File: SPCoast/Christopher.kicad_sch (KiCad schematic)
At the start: 42 parts, among them SW9813 813, SW9815 815, SW9817 817, SW9900 815A

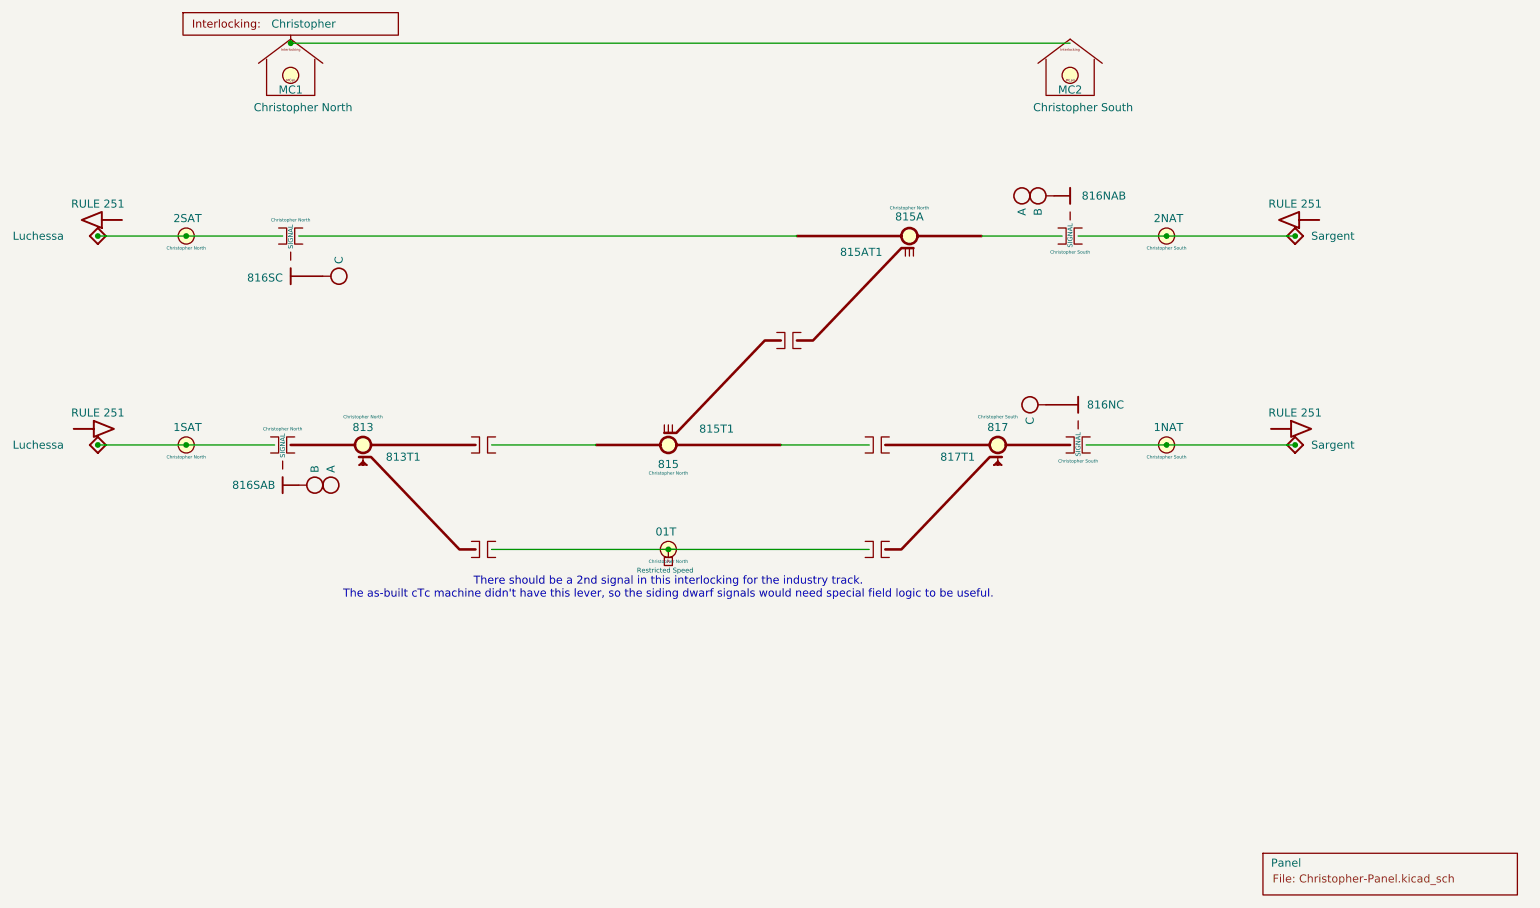
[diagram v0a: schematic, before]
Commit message: chore(kicad): SPCoast symbols refreshed, field attribute visibility, no-connects on unused pins (owner's edit, baseline)
Owner, 2026-10-08: updated symbols from the libraries (the field pin direction flip, InterlockingPlant
61269e0), adjusted attribute visibility, added 22 no-connect markers on unused pins.

Verified (committed as saved, no edits):
- 485 components, 648 nets; every net identical to the previous commit.
- ERC 53 -> 20 messages (13 errors, 7 warnings). Remaining: unconnected HOUSE H / aux MC pins
  (Gilroy Caltrain, Luchessa, Watsonville); Corporal SW11901 still Railroad:Switch_HandThrow (not in
  the library) with open N/R legs; Sargent switch 1 open N/R legs; Christopher Panel U10029 A6 open
  while lamp LMP10093 carries a no-connect; 5 inherited wire stubs.
- Every instance path starts at the root uuid.

Co-Authored-By: Claude Opus 5.5 <noreply@anthropic.com>
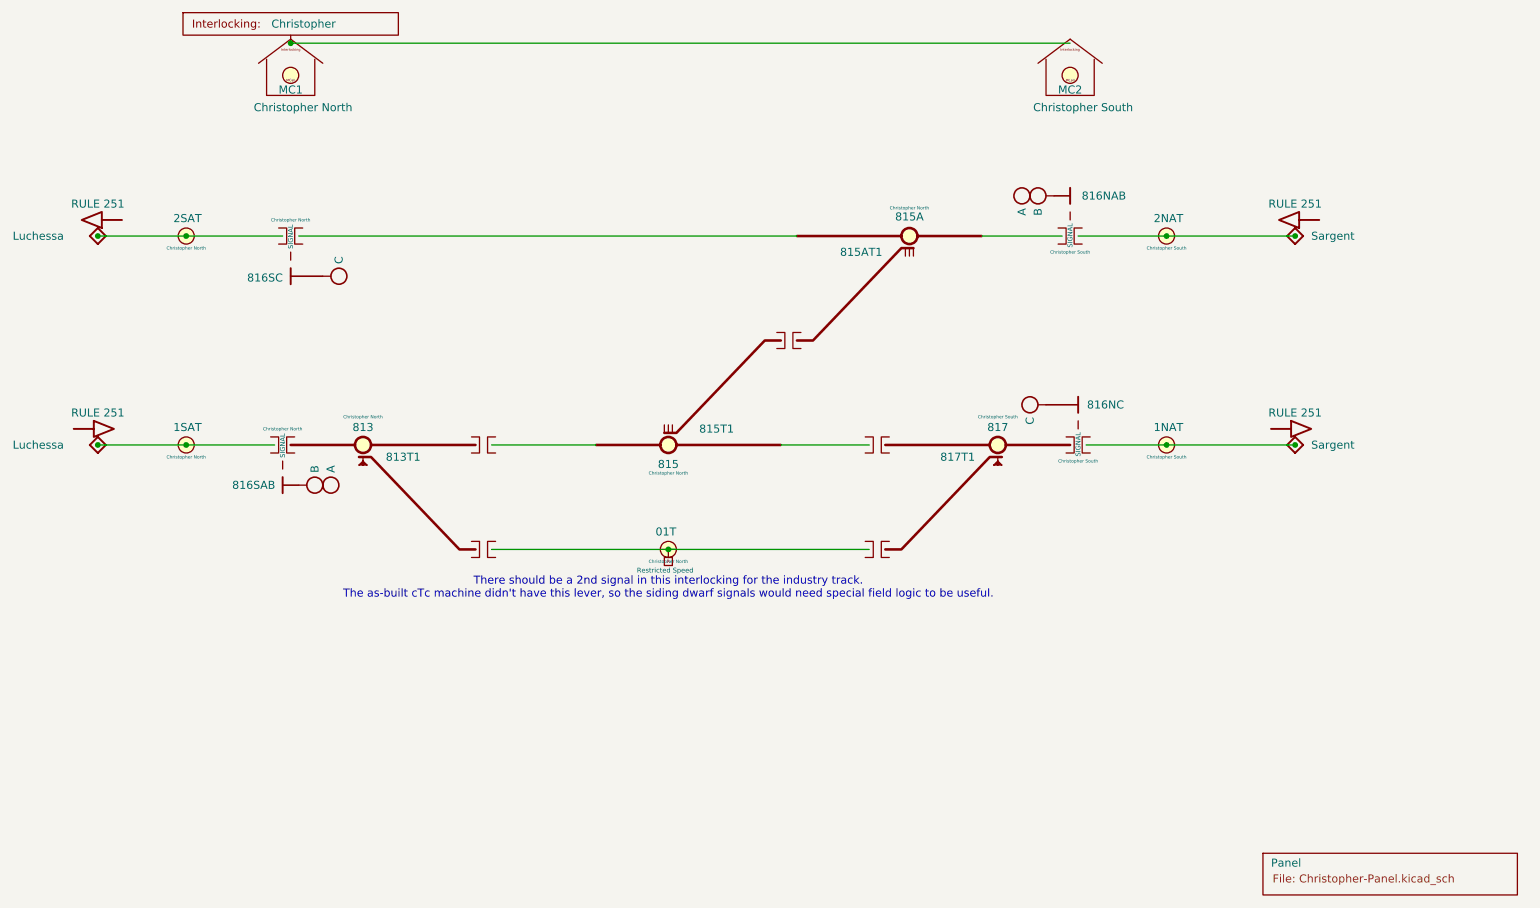
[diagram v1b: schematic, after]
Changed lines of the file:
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@@
 		)
 		(property "Milepost" "81.6"
-			(at 195.58 47.63 0)
+			(at 195.58 47.625 0)
 			(hide yes)
 			(show_name no)
@@
 		)
 		(property "CP" "Christopher North"
-			(at 55.88 102.23 0)
+			(at 55.88 102.235 0)
 			(show_name no)
 			(do_not_autoplace no)
@@
 		)
 		(property "CP" "Christopher North"
-			(at 132.08 104.78 0)
+			(at 132.08 104.775 0)
 			(show_name no)
 			(do_not_autoplace no)
@@
 			(at 139.7 97.79 0)
 			(show_name no)
-			(do_not_autoplace no)
+			(do_not_autoplace yes)
 			(effects
 				(font
@@
 		)
 		(property "Role" "APPLIANCE"
-			(at 132.08 100.33 0)
+			(at 123.825 92.71 0)
 			(hide yes)
 			(show_name no)
@@
 		)
 		(property "Kind" "SWITCH_REMOTE"
-			(at 132.08 100.33 0)
+			(at 126.365 94.615 0)
 			(hide yes)
 			(show_name no)
@@
 			)
 		)
+		(property "Indications" ""
+			(at 145.415 99.695 0)
+			(show_name no)
+			(do_not_autoplace no)
+			(effects
+				(font
+					(size 0.508 0.508)
+				)
+			)
+		)
 		(pin "2"
 		)
@@
 		)
 		(property "CP" "Christopher North"
-			(at 83.82 95.88 0)
+			(at 83.82 95.885 0)
 			(show_name no)
 			(do_not_autoplace no)
@@
 		)
 		(property "TC" "${VALUE}T1"
-			(at 90.17 102.23 0)
+			(at 90.17 102.235 0)
 			(show_name no)
 			(do_not_autoplace no)
@@
 		)
 		(property "Role" "APPLIANCE"
-			(at 83.82 100.33 0)
+			(at 76.835 106.68 0)
 			(hide yes)
 			(show_name no)
@@
 		)
 		(property "Kind" "SWITCH_LOCK"
-			(at 83.82 100.33 0)
+			(at 78.105 104.775 0)
 			(hide yes)
 			(show_name no)
@@
 			)
 		)
+		(property "Indications" ""
+			(at 97.155 100.965 0)
+			(show_name no)
+			(do_not_autoplace no)
+			(effects
+				(font
+					(size 0.508 0.508)
+				)
+			)
+		)
 		(pin "3"
 		)
@@
 		)
 		(property "CP" "Christopher North"
-			(at 132.08 118.74 0)
+			(at 132.08 118.745 0)
 			(show_name no)
 			(do_not_autoplace no)
@@
 		)
 		(property "Milepost" "81.3"
-			(at 72.39 47.63 0)
+			(at 72.39 47.625 0)
 			(hide yes)
 			(show_name no)
@@
 		)
 		(property "CP" "Christopher North"
-			(at 170.18 62.86 0)
+			(at 170.18 62.865 0)
 			(show_name no)
 			(do_not_autoplace no)
@@
 			(at 162.56 69.85 0)
 			(show_name no)
-			(do_not_autoplace no)
+			(do_not_autoplace yes)
 			(effects
 				(font
@@
 		)
 		(property "Role" "APPLIANCE"
-			(at 170.18 67.31 0)
+			(at 178.435 74.93 0)
 			(hide yes)
 			(show_name no)
@@
 		)
 		(property "Kind" "SWITCH_REMOTE"
-			(at 170.18 67.31 0)
+			(at 175.895 73.025 0)
 			(hide yes)
 			(show_name no)
@@
 			)
 		)
+		(property "Indications" ""
+			(at 156.845 67.945 0)
+			(show_name no)
+			(do_not_autoplace no)
+			(effects
+				(font
+					(size 0.508 0.508)
+				)
+			)
+		)
 		(pin "2"
 		)
@@
 		)
 		(property "CP" "Christopher South"
-			(at 210.82 69.21 0)
+			(at 210.82 69.215 0)
 			(show_name no)
 			(do_not_autoplace no)
@@
 		)
 		(property "CP" "Christopher South"
-			(at 210.82 102.23 0)
+			(at 210.82 102.235 0)
 			(show_name no)
 			(do_not_autoplace no)
@@
 		)
 		(property "CP" "Christopher South"
-			(at 184.15 95.88 0)
+			(at 184.15 95.885 0)
 			(show_name no)
 			(do_not_autoplace no)
@@
 		)
 		(property "TC" "${VALUE}T1"
-			(at 177.8 102.23 0)
+			(at 177.8 102.235 0)
 			(show_name no)
 			(do_not_autoplace no)
@@
 		)
 		(property "Role" "APPLIANCE"
-			(at 184.15 100.33 0)
+			(at 191.135 106.68 0)
 			(hide yes)
 			(show_name no)
@@
 		)
 		(property "Kind" "SWITCH_LOCK"
-			(at 184.15 100.33 0)
+			(at 189.865 104.775 0)
 			(hide yes)
 			(show_name no)
@@
 			)
 		)
+		(property "Indications" ""
+			(at 170.815 100.965 0)
+			(show_name no)
+			(do_not_autoplace no)
+			(effects
+				(font
+					(size 0.508 0.508)
+				)
+			)
+		)
 		(pin "3"
 		)
@@
 		)
 		(property "CP" "Christopher North"
-			(at 55.88 69.21 0)
+			(at 55.88 69.215 0)
 			(show_name no)
 			(do_not_autoplace no)

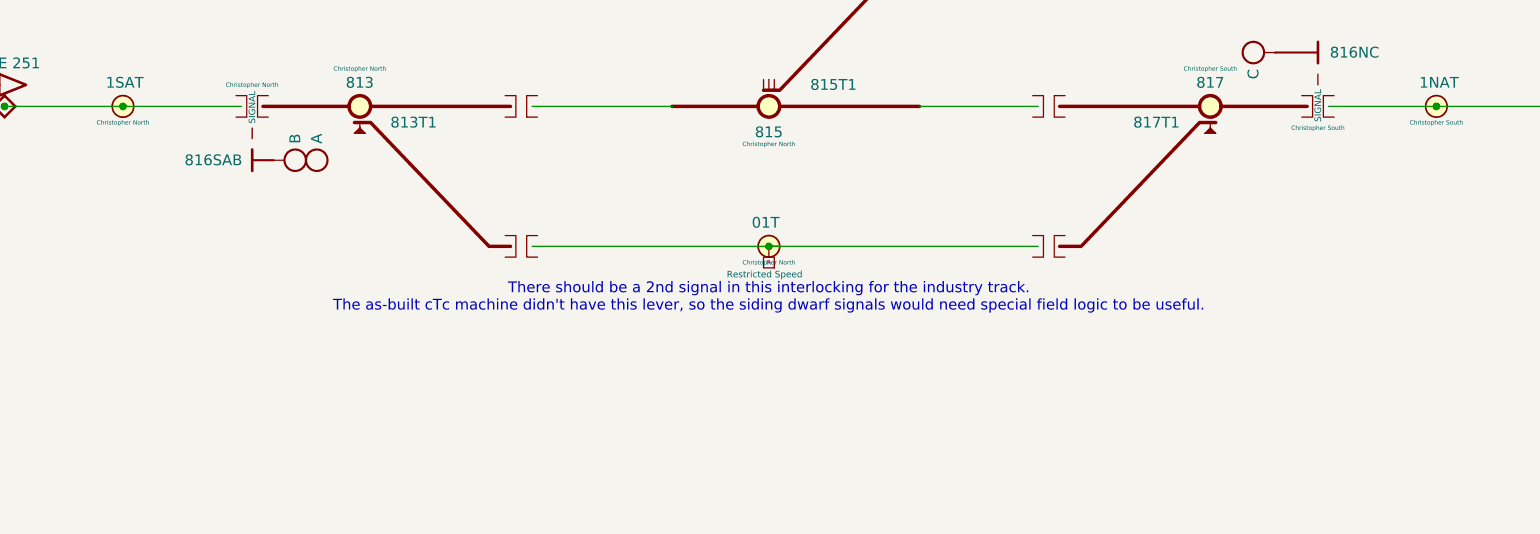
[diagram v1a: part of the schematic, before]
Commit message: fix(kicad): SPCoast ERC clean: Corporal SW11901 to Switch_Manual_Sensed, Christopher lamp fixed, no-connects (owner's edit, baseline)
Owner, 2026-10-08. Corporal and Sargent's industry tracks (the beet loader) join each other outside
CTC: dark track, no routes, no NextCP.

Verified (committed as saved, no edits): 485 components, 648 nets; ERC 0 errors, 0 warnings.

Co-Authored-By: Claude Opus 5.5 <noreply@anthropic.com>
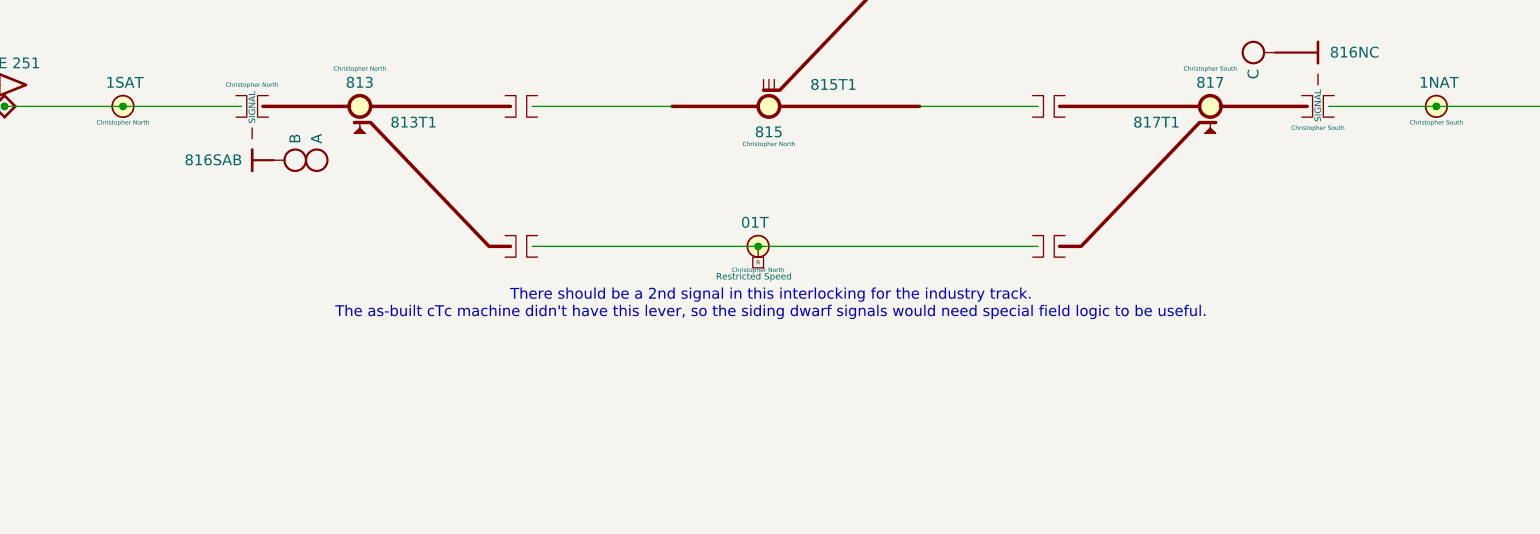
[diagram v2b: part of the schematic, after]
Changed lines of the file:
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@@
 	(text "There should be a 2nd signal in this interlocking for the industry track.\nThe as-built cTc machine didn't have this lever, so the siding dwarf signals would need special field logic to be useful."
 		(exclude_from_sim no)
-		(at 132.08 122.936 0)
+		(at 132.334 123.698 0)
 		(effects
 			(font
@@
 	)
 	(junction
-		(at 132.08 116.84)
+		(at 231.14 67.31)
 		(diameter 0)
 		(color 0 0 0 0)
 	)
 	(junction
-		(at 231.14 67.31)
+		(at 130.81 116.84)
 		(diameter 0)
 		(color 0 0 0 0)
@@
 	(wire
 		(pts
-			(xy 132.08 116.84) (xy 163.83 116.84)
+			(xy 104.14 116.84) (xy 163.83 116.84)
 		)
 		(stroke
@@
 	(wire
 		(pts
-			(xy 104.14 116.84) (xy 132.08 116.84)
-		)
-		(stroke
-			(width 0.4064)
-			(type dash)
-			(color 72 72 72 1)
-		)
-	)
-	(wire
-		(pts
 			(xy 72.39 36.83) (xy 195.58 36.83)
 		)
@@
 		(stroke
 			(width 0.4064)
-			(type default)
-		)
-	)
-	(wire
-		(pts
-			(xy 132.08 116.84) (xy 133.35 116.84)
-		)
-		(stroke
-			(width 0)
 			(type default)
 		)
@@
 	(symbol
 		(lib_id "Railroad:Rule105-RestrictedSpeed")
-		(at 132.08 119.38 180)
+		(at 130.81 119.38 180)
 		(unit 1)
 		(body_style 1)
@@
 		(dnp no)
 		(property "Reference" "DOT9005"
-			(at 137.795 120.015 0)
+			(at 136.525 120.015 0)
 			(hide yes)
 			(show_name no)
@@
 		)
 		(property "Value" "Restricted Speed"
-			(at 131.572 120.142 0)
+			(at 130.302 120.396 0)
 			(show_name no)
 			(do_not_autoplace yes)
@@
 		)
 		(property "Footprint" ""
-			(at 135.255 119.38 0)
+			(at 133.985 119.38 0)
 			(hide yes)
 			(show_name no)
@@
 		)
 		(property "Datasheet" ""
-			(at 135.255 119.38 0)
+			(at 133.985 119.38 0)
 			(hide yes)
 			(show_name no)
@@
 		)
 		(property "Description" "Restricted speed: Standard Code Rule 105, GCOR 6.28: Movement on Other Than Main Track. This is the foundational rule governing most industrial tracks. It mandates that trains or engines must move at a speed that allows them to stop within half the range of vision short of a train, engine, car, stop signal, derail, or switch improperly lined. It also requires crew members to look out for track obstructions"
-			(at 135.255 114.935 0)
+			(at 133.985 114.935 0)
 			(hide yes)
 			(show_name no)
@@
 		)
 		(property "Kind" "RULE_105"
-			(at 132.08 116.84 0)
+			(at 130.81 116.84 0)
 			(hide yes)
 			(show_name no)
@@
 		)
 		(property "Direction" "BOTH"
-			(at 137.795 118.11 0)
+			(at 136.525 118.11 0)
 			(hide yes)
 			(show_name no)
@@
 		)
 		(property "Role" "POLICY"
-			(at 132.08 119.38 0)
+			(at 130.81 119.38 0)
 			(hide yes)
 			(show_name no)
@@
 	(symbol
 		(lib_id "Railroad:Track Circuit")
-		(at 132.08 116.84 0)
+		(at 130.81 116.84 0)
 		(unit 1)
 		(body_style 1)
@@
 		(dnp no)
 		(property "Reference" "TC9005"
-			(at 132.08 112.4 0)
+			(at 130.81 112.4 0)
 			(hide yes)
 			(show_name no)
@@
 		)
 		(property "Value" "01T"
-			(at 130.05 114.05 0)
+			(at 128.78 114.05 0)
 			(show_name no)
 			(do_not_autoplace no)
@@
 		)
 		(property "Footprint" ""
-			(at 132.08 116.84 0)
+			(at 130.81 116.84 0)
 			(hide yes)
 			(show_name no)
@@
 		)
 		(property "Datasheet" ""
-			(at 132.08 116.84 0)
+			(at 130.81 116.84 0)
 			(hide yes)
 			(show_name no)
@@
 		)
 		(property "Description" ""
-			(at 132.08 116.84 0)
+			(at 130.81 116.84 0)
 			(hide yes)
 			(show_name no)
@@
 		)
 		(property "CP" "Christopher North"
-			(at 132.08 118.745 0)
+			(at 130.81 119.634 0)
 			(show_name no)
 			(do_not_autoplace no)
@@
 		)
 		(property "Role" "APPLIANCE"
-			(at 132.08 116.84 0)
+			(at 130.81 116.84 0)
 			(hide yes)
 			(show_name no)
@@
 		)
 		(property "Kind" "TRACK_CIRCUIT"
-			(at 132.08 116.84 0)
-			(hide yes)
-			(show_name no)
+			(at 130.81 116.84 0)
+			(hide yes)
+			(show_name no)

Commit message: feat(spcoast): every sheet on the four Railroad libraries (checkpoint step 6, mechanical half)
By SPCoast/edits/2026-10-12-migrate-libraries.py, run once with KiCad closed: 483 instances
remapped across 16 sheets, embedded definitions replaced by the library blocks, instance fields
synced (Kind, ControlToken, Vital, NormalIs, Chain, Index dropped; Indications renamed
IndicationCeiling; Hold_ms renamed hold_ms; a pixel's Index became its Address; Rulebook kept
on the four Luchessa markers because the compiler still reads it), and 22 units added at the
same position for the plates and devices that are multi-unit now. Owner's choices: every plant
head CPL; Sargent's semaphore UQ; the 0x27 PCA9685 as PWM; the office MAX7313s as the
SPCoastcTc variant. Left by hand: the two AUXILIARY_TRAFFIC markers on Watsonville (retired).

Verified (production/migration-gate.txt, netlist_diff.py against pre-migration.net): office
and local plates and all chips keep their connectivity; 14 nets lost, all on Sargent, where
the six field devices (DevSW13001, 13004 to 13007, 13012) have new pin positions and must be
re-wired by hand. ERC: lib_symbol_issues 492 before (unregistered libraries) to 2 after (the
retired markers); the 29 unconnected pins are those devices and their chip pins.

Co-Authored-By: Claude Fable 5.1 <noreply@anthropic.com>
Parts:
- B9001, B9002, B9003, B9008, B9009: symbol Railroad:IRJ -> Railroad-Trackplan:IRJ
- B9004, B9005, B9006, B9007: symbol Railroad:IRJ-Signal -> Railroad-Trackplan:IRJ-Signal
- CP9001, CP9002, CP9003, CP9004: symbol Railroad:NextCP -> Railroad-Trackplan:NextCP
- DOT9001, DOT9004: symbol Railroad:Rule251-DoT-Right -> Railroad-Trackplan:Rule251-DoT-Right
- DOT9002, DOT9003: symbol Railroad:Rule251-DoT-Left -> Railroad-Trackplan:Rule251-DoT-Left
- DOT9005: symbol Railroad:Rule105-RestrictedSpeed -> Railroad-Trackplan:Rule105-RestrictedSpeed
- H9003, H9005, H9006, H9008, H9009, H9010: symbol Railroad:Signal Head - CL -> Railroad-Trackplan:Signal Head - CPL; Appliance (none) -> head; Kind HEAD -> (none); Style (none) -> CPL
- HOUSE9001, HOUSE9003: symbol Railroad:MAIN HOUSE -> Railroad-Trackplan:MAIN HOUSE
- MC9001, MC9002: symbol Railroad:MaintainerCall -> Railroad-Trackplan:MaintainerCall; Appliance (none) -> lamp; Kind MAINTAINER_CALL -> (none); Style (none) -> maintainer_call
- Plant9001: symbol Railroad:Interlocking -> Railroad-Trackplan:Interlocking
- S9003, S9005: symbol Railroad:Mast_Single -> Railroad-Trackplan:Mast_Single; Appliance (none) -> mast; Kind MAST_SINGLE -> (none); Style (none) -> single
- S9004, S9006: symbol Railroad:Mast_Double -> Railroad-Trackplan:Mast_Double; Appliance (none) -> mast; Kind MAST_DOUBLE -> (none); Style (none) -> double
- SW9813, SW9817: symbol Railroad:Switch_Lock -> Railroad-Trackplan:Switch_Lock; Appliance (none) -> switch; Kind SWITCH_LOCK -> (none); Style (none) -> lock
- SW9815, SW9900: symbol Railroad:Switch_Powered -> Railroad-Trackplan:Switch_Powered; Appliance (none) -> switch; Kind SWITCH_REMOTE -> (none); Style (none) -> powered
- TC9001, TC9002, TC9003, TC9004, TC9005: symbol Railroad:Track Circuit -> Railroad-Trackplan:Track Circuit; Appliance (none) -> track_circuit; Kind TRACK_CIRCUIT -> (none)
